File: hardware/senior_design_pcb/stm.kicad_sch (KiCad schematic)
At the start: 65 parts, among them J1 SBH11-PBPC-D05-ST-BK, J10 Screw_Terminal_01x06, J11 Conn_02x08_Odd_Even, J12 Conn_01x05_Socket, J2 USB_C_Receptacle_USB2.0_16P, J3 Conn_01x02_Socket, J4 Conn_01x03_Socket, J5 Conn_01x05_Socket, J6 Conn_01x05_Socket, J7 Conn_01x02_Socket, J8 Conn_01x03_Socket, J9 Screw_Terminal_01x06, SW1 SW_Push, SW2 SW_Push, SW3 SW_Push, SW4 SW_Push, U1 FT232RL, U2 STM32F091RCTx, U3 LD1117S33TR_SOT223, X1 32.768kHz(12.5pF), X2 8MHz(20pF)

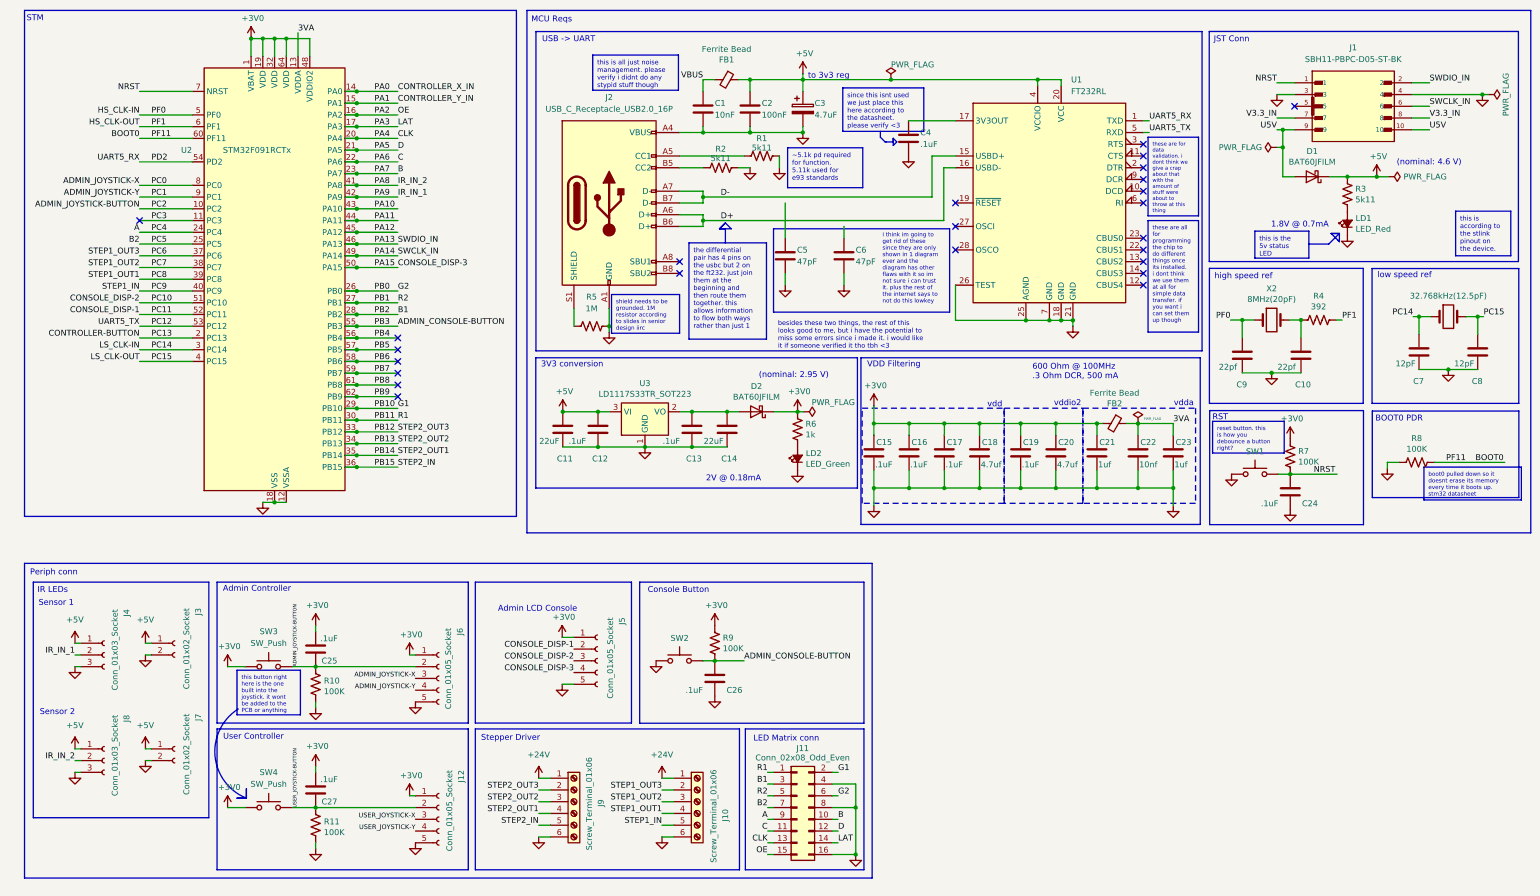
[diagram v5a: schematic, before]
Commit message: added pcb, removed schematic level
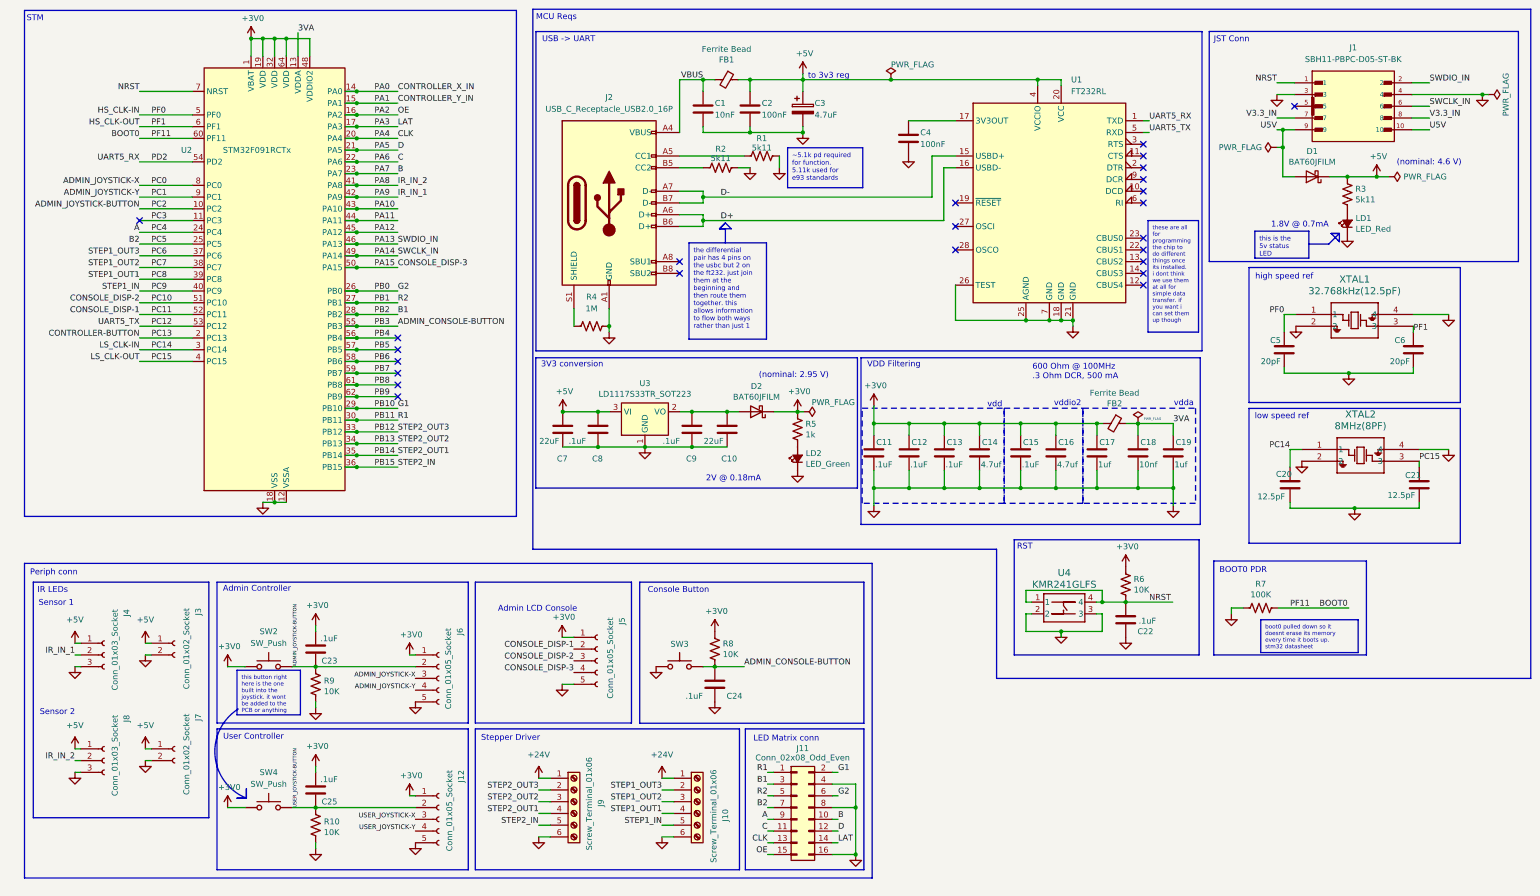
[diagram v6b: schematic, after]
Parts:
- removed C5, C6: 47pF, Capacitor_SMD:C_0805_2012Metric_Pad1.15x1.40mm_HandSolder, symbol Device:C
- removed R4: 392, Resistor_SMD:R_0805_2012Metric_Pad1.15x1.40mm_HandSolder, symbol Device:R_US
- removed SW1: SW_Push, Button_Switch_SMD:SW_SPST_PTS645, symbol Switch:SW_Push
- removed X1: 32.768kHz(12.5pF), Crystal:Crystal_SMD_3225-4Pin_3.2x2.5mm, symbol Device:Crystal
- removed X2: 8MHz(20pF), Crystal:Crystal_SMD_3225-4Pin_3.2x2.5mm, symbol Device:Crystal
- added U4: KMR241GLFS, General Library:KMR241G-RESET-BUTTON, symbol KMR241G-RESET-BUTTON:KMR241GLFS
- added XTAL1: 32.768kHz(12.5pF), Sr_ Design:ECS - CRYSTAL 32.7680KHZ 6PF SMD, symbol ECS-CRYSTAL 8MHZ 8PF SMD:ECS-80-8-33Q-ADS
- added XTAL2: 8MHz(8PF), Sr_ Design:ECS-CRYSTAL 8MHZ 8PF SMD, symbol ECS-CRYSTAL 8MHZ 8PF SMD:ECS-80-8-33Q-ADS
- C1, C2, C3: footprint Capacitor_SMD:C_0805_2012Metric_Pad1.15x1.40mm_HandSolder -> Capacitor_SMD:C_0805_2012Metric_Pad1.18x1.45mm_HandSolder
- C10: renamed from C14; footprint Capacitor_SMD:C_0805_2012Metric_Pad1.15x1.40mm_HandSolder -> Capacitor_SMD:C_0805_2012Metric_Pad1.18x1.45mm_HandSolder
- C11: renamed from C15; footprint Capacitor_SMD:C_0805_2012Metric_Pad1.15x1.40mm_HandSolder -> Capacitor_SMD:C_0805_2012Metric_Pad1.18x1.45mm_HandSolder
- C12: renamed from C16; footprint Capacitor_SMD:C_0805_2012Metric_Pad1.15x1.40mm_HandSolder -> Capacitor_SMD:C_0805_2012Metric_Pad1.18x1.45mm_HandSolder
- C13: renamed from C17; footprint Capacitor_SMD:C_0805_2012Metric_Pad1.15x1.40mm_HandSolder -> Capacitor_SMD:C_0805_2012Metric_Pad1.18x1.45mm_HandSolder
- C14: renamed from C18; footprint Capacitor_SMD:C_0805_2012Metric_Pad1.15x1.40mm_HandSolder -> Capacitor_SMD:C_0805_2012Metric_Pad1.18x1.45mm_HandSolder
- C15: renamed from C19; footprint Capacitor_SMD:C_0805_2012Metric_Pad1.15x1.40mm_HandSolder -> Capacitor_SMD:C_0805_2012Metric_Pad1.18x1.45mm_HandSolder
- C16: renamed from C20; footprint Capacitor_SMD:C_0805_2012Metric_Pad1.15x1.40mm_HandSolder -> Capacitor_SMD:C_0805_2012Metric_Pad1.18x1.45mm_HandSolder
- C17: renamed from C21; footprint Capacitor_SMD:C_0805_2012Metric_Pad1.15x1.40mm_HandSolder -> Capacitor_SMD:C_0805_2012Metric_Pad1.18x1.45mm_HandSolder
- C18: renamed from C22; footprint Capacitor_SMD:C_0805_2012Metric_Pad1.15x1.40mm_HandSolder -> Capacitor_SMD:C_0805_2012Metric_Pad1.18x1.45mm_HandSolder
- C19: renamed from C23; footprint Capacitor_SMD:C_0805_2012Metric_Pad1.15x1.40mm_HandSolder -> Capacitor_SMD:C_0805_2012Metric_Pad1.18x1.45mm_HandSolder
- C20: renamed from C7; value 12pF -> 12.5pF; footprint Capacitor_SMD:C_0805_2012Metric_Pad1.15x1.40mm_HandSolder -> Capacitor_SMD:C_0805_2012Metric_Pad1.18x1.45mm_HandSolder
- C21: renamed from C8; value 12pF -> 12.5pF; footprint Capacitor_SMD:C_0805_2012Metric_Pad1.15x1.40mm_HandSolder -> Capacitor_SMD:C_0805_2012Metric_Pad1.18x1.45mm_HandSolder
- C22: renamed from C24; footprint Capacitor_SMD:C_0805_2012Metric_Pad1.15x1.40mm_HandSolder -> Capacitor_SMD:C_0805_2012Metric_Pad1.18x1.45mm_HandSolder
- C23: renamed from C25; footprint Capacitor_SMD:C_0805_2012Metric_Pad1.15x1.40mm_HandSolder -> Capacitor_SMD:C_0805_2012Metric_Pad1.18x1.45mm_HandSolder
- C24: renamed from C26; footprint Capacitor_SMD:C_0805_2012Metric_Pad1.15x1.40mm_HandSolder -> Capacitor_SMD:C_0805_2012Metric_Pad1.18x1.45mm_HandSolder
- C25: renamed from C27; footprint Capacitor_SMD:C_0805_2012Metric_Pad1.15x1.40mm_HandSolder -> Capacitor_SMD:C_0805_2012Metric_Pad1.18x1.45mm_HandSolder
- C4: value .1uF -> 100nF; footprint Capacitor_SMD:C_0805_2012Metric_Pad1.15x1.40mm_HandSolder -> Capacitor_SMD:C_0805_2012Metric_Pad1.18x1.45mm_HandSolder
- C5: renamed from C9; value 22pf -> 20pF; footprint Capacitor_SMD:C_0805_2012Metric_Pad1.15x1.40mm_HandSolder -> Capacitor_SMD:C_0805_2012Metric_Pad1.18x1.45mm_HandSolder
- C6: renamed from C10; value 22pf -> 20pF; footprint Capacitor_SMD:C_0805_2012Metric_Pad1.15x1.40mm_HandSolder -> Capacitor_SMD:C_0805_2012Metric_Pad1.18x1.45mm_HandSolder
- C7: renamed from C11; footprint Capacitor_SMD:C_0805_2012Metric_Pad1.15x1.40mm_HandSolder -> Capacitor_SMD:C_0805_2012Metric_Pad1.18x1.45mm_HandSolder
- C8: renamed from C12; footprint Capacitor_SMD:C_0805_2012Metric_Pad1.15x1.40mm_HandSolder -> Capacitor_SMD:C_0805_2012Metric_Pad1.18x1.45mm_HandSolder
- C9: renamed from C13; footprint Capacitor_SMD:C_0805_2012Metric_Pad1.15x1.40mm_HandSolder -> Capacitor_SMD:C_0805_2012Metric_Pad1.18x1.45mm_HandSolder
- D1, D2: footprint Diode_SMD:D_SOD-323 -> Diode_SMD:D_SOD-323_HandSoldering
- FB1, FB2: footprint Inductor_SMD:L_0805_2012Metric_Pad1.15x1.40mm_HandSolder -> Inductor_SMD:L_0805_2012Metric_Pad1.05x1.20mm_HandSolder
- J1: footprint SBH11-PBPC-D05-ST-BK:SULLINS_SBH11-PBPC-D05-ST-BK -> General Library:jtag_conn
- J10, J9: footprint (none) -> Connector_JST:JST_EH_S6B-EH_1x06_P2.50mm_Horizontal
- J12, J5, J6: footprint (none) -> Connector_JST:JST_EH_S5B-EH_1x05_P2.50mm_Horizontal
- J2: footprint (none) -> Sr_ Design:USB-C-PORT-2
- J3, J7: footprint (none) -> Connector_JST:JST_EH_S2B-EH_1x02_P2.50mm_Horizontal
- J4, J8: footprint (none) -> Connector_JST:JST_EH_S3B-EH_1x03_P2.50mm_Horizontal
- R1, R2: footprint Resistor_SMD:R_0805_2012Metric -> Resistor_SMD:R_0805_2012Metric_Pad1.20x1.40mm_HandSolder
- R10: renamed from R11; value 100K -> 10K; footprint Resistor_SMD:R_0805_2012Metric_Pad1.15x1.40mm_HandSolder -> Resistor_SMD:R_0805_2012Metric_Pad1.20x1.40mm_HandSolder
- R3: footprint Resistor_SMD:R_0805_2012Metric_Pad1.15x1.40mm_HandSolder -> Resistor_SMD:R_0805_2012Metric_Pad1.20x1.40mm_HandSolder
- R4: renamed from R5; footprint Resistor_SMD:R_0805_2012Metric -> Resistor_SMD:R_0805_2012Metric_Pad1.20x1.40mm_HandSolder
- R5: renamed from R6; footprint Resistor_SMD:R_0805_2012Metric_Pad1.15x1.40mm_HandSolder -> Resistor_SMD:R_0805_2012Metric_Pad1.20x1.40mm_HandSolder
- R6: renamed from R7; value 100K -> 10K; footprint Resistor_SMD:R_0805_2012Metric_Pad1.15x1.40mm_HandSolder -> Resistor_SMD:R_0805_2012Metric_Pad1.20x1.40mm_HandSolder
- R7: renamed from R8; footprint Resistor_SMD:R_0805_2012Metric_Pad1.15x1.40mm_HandSolder -> Resistor_SMD:R_0805_2012Metric_Pad1.20x1.40mm_HandSolder
- R8: renamed from R9; value 100K -> 10K; footprint Resistor_SMD:R_0805_2012Metric_Pad1.15x1.40mm_HandSolder -> Resistor_SMD:R_0805_2012Metric_Pad1.20x1.40mm_HandSolder
- R9: renamed from R10; value 100K -> 10K; footprint Resistor_SMD:R_0805_2012Metric_Pad1.15x1.40mm_HandSolder -> Resistor_SMD:R_0805_2012Metric_Pad1.20x1.40mm_HandSolder
- renumbered SW3 to SW2, SW2 to SW3
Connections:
- net GND: now also U4.2, U4.3, XTAL1.2, XTAL1.4, XTAL2.2, XTAL2.4; no longer J2.A4 (VBUS), J2.A9 (VBUS), J2.B4 (VBUS), J2.B9 (VBUS)
- net HS_CLK-IN: now also XTAL1.1
- net HS_CLK-OUT: now also C6.1, XTAL1.3
- net LS_CLK-IN: now also XTAL2.1
- net LS_CLK-OUT: now also XTAL2.3
- net NRST: now also U4.1, U4.4
- net VBUS: now also J2.A4 (VBUS), J2.A9 (VBUS), J2.B4 (VBUS), J2.B9 (VBUS)
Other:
- moved on the sheet: C20, C21, C22, C24, C5, C6, R6, R7, R8, SW3
